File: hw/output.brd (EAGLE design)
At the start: 60.6 x 71.1 mm, 22 parts, among them Q1 MOSFET-NCHANNELFDD8780, Q2 MOSFET-NCHANNELFDD8780, U3 TMP102

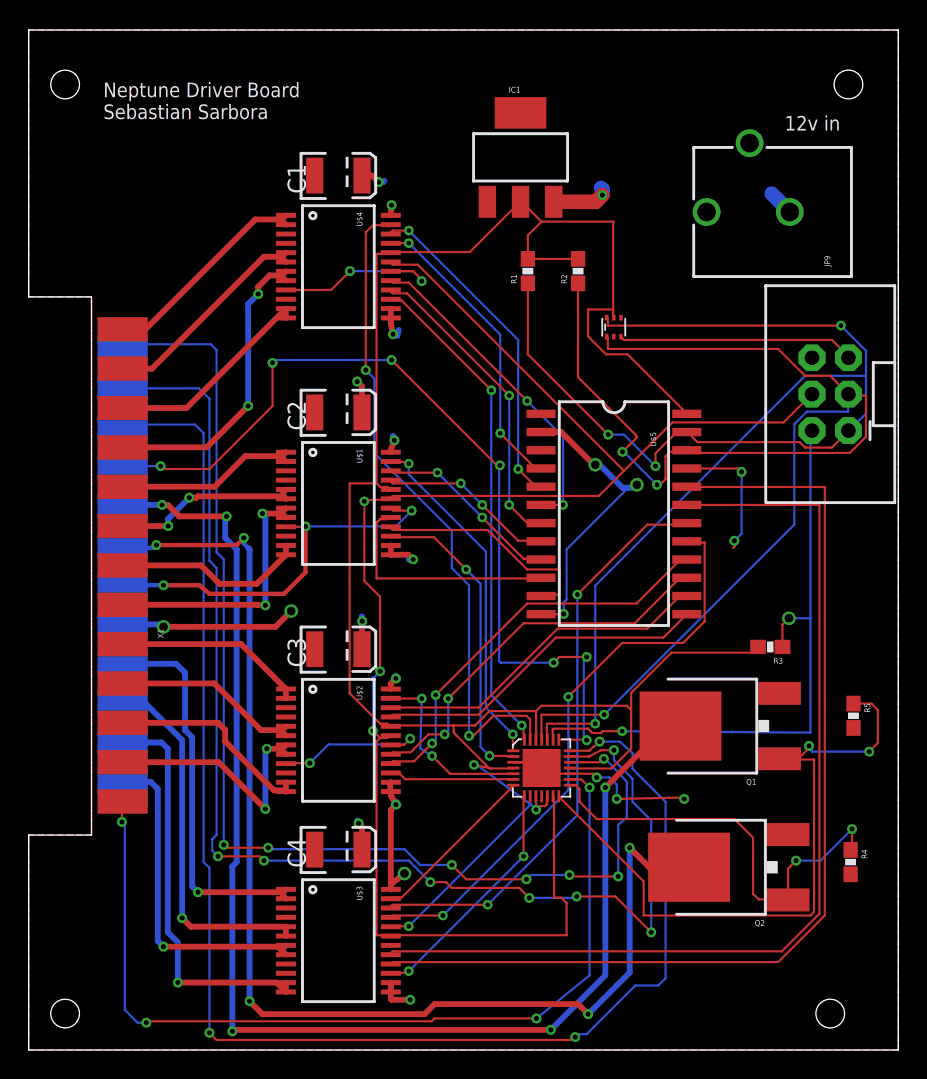
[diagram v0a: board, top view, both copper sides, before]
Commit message: Consolidated output board to use single control IC (CY8C9540A), removed servo pwm lines for this revision.
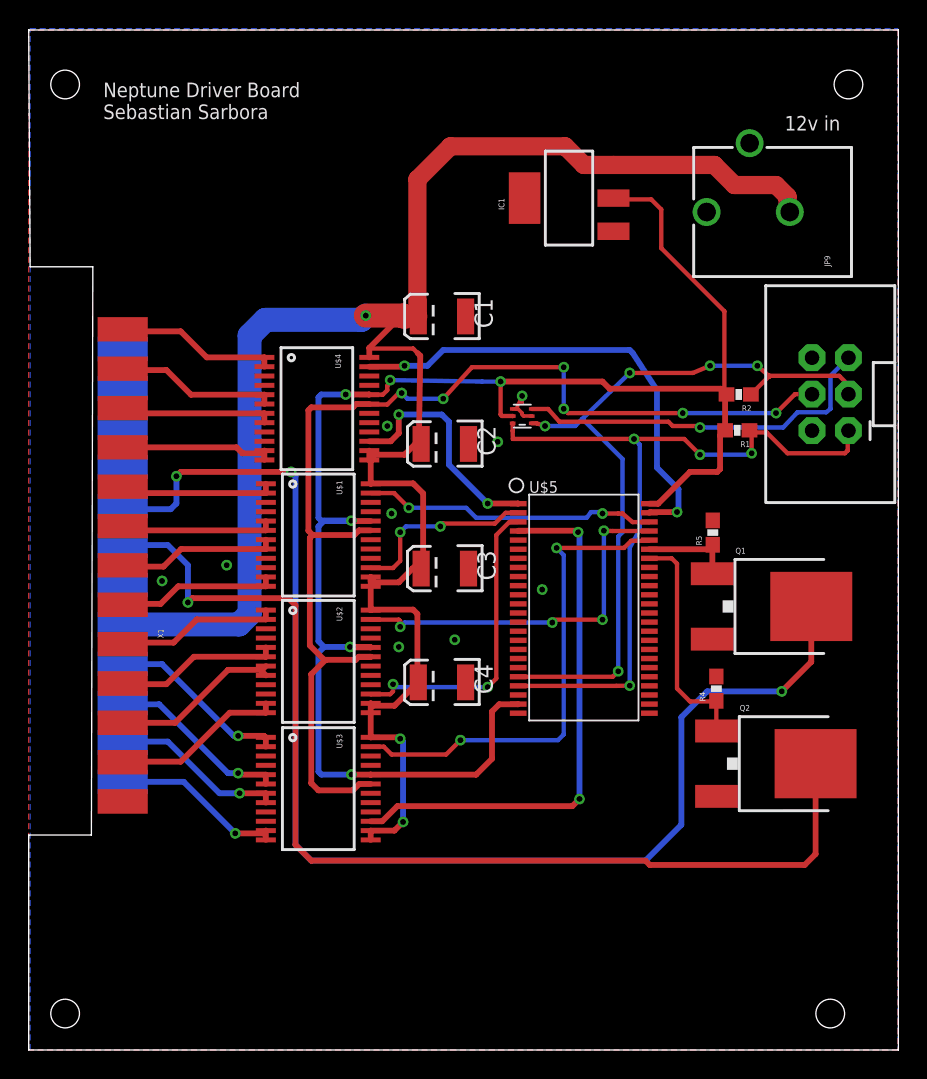
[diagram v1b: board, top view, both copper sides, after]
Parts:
- removed R3: 1K, SparkFun-Resistors:0603-RES
- removed U2: (no value), SparkFun-DigitalIC:QFN-28
- U$5: value PCF8575C -> CY8C9540A; device SparkFun-DigitalIC:SO-24DW -> SpaceY:48-SSOP-CY
- moved R1 18.3 mm to (49.4, 43.2), turned to 180 degrees
- moved R5 16.1 mm to (47.7, 36.1), turned to 90 degrees
- moved R4 15.3 mm to (47.9, 25.2), turned to 90 degrees
- moved R2 14.1 mm to (49.5, 45.7), turned to 180 degrees
- moved C4 13.7 mm to (28.8, 25.6), turned to 180 degrees
- moved C1 12.2 mm to (28.8, 51.1), turned to 180 degrees
- moved U$3 10.7 mm to (20.2, 18.2)
- moved Q1 10.2 mm to (53.0, 30.9), turned to 270 degrees
- moved U$4 10.0 mm to (20.1, 44.7)
- moved C3 9.31 mm to (29.0, 33.6), turned to 180 degrees
- moved Q2 9.16 mm to (53.3, 20.0), turned to 270 degrees
- moved U3 8.90 mm to (34.4, 44.2), turned to 90 degrees
- moved C2 7.74 mm to (29.0, 42.2), turned to 180 degrees
- moved U$5 7.21 mm to (38.7, 31.1), turned to 0 degrees
- moved U$2 5.68 mm to (20.2, 27.1)
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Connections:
- removed net N$1: U$5.1
- removed net N$42: U2.11
- removed net N$43: U2.9
- net AIN1: no longer U$5.4
- net AIN2: no longer U$5.5
- net B1: now also X1.4; no longer X1.3
- net B2: now also X1.3; no longer X1.4
- net BIN1: no longer U$5.6
- net BIN2: no longer U$5.7
- net CIN1: no longer U$5.8
- net CIN2: no longer U$5.9
- net D1: now also X1.8; no longer X1.7
- net D2: now also X1.7; no longer X1.8
- net DIN1: no longer U$5.10
- net DIN2: no longer U$5.11
- net EIN1: no longer U$5.13
- net EIN2: no longer U$5.14
- net F1: now also X1.12; no longer X1.11
- net F2: now also X1.11; no longer X1.12
- net FIN1: no longer U$5.15
- net FIN2: no longer U$5.16
- net GIN1: no longer U$5.17
- net GIN2: no longer U$5.18
- net GND: now also U$5.13, U$5.24, U$5.26; no longer U$5.12, U$5.2, U$5.21, U$5.3, U2.17, U2.29, U2.3
- net H1: now also X1.25; no longer X1.24
- net H2: now also X1.24; no longer X1.25
- net HIN1: no longer U$5.19
- net HIN2: no longer U$5.20
- net LED1: now also U$5.43; no longer U2.14
- net LED2: now also U$5.42; no longer U2.15
- net PWM_A: now also U$5.47; no longer U2.27
- net PWM_B: now also U$5.1; no longer U2.28
- net PWM_C: now also U$5.46; no longer U2.1
- net PWM_D: now also U$5.2; no longer U2.2
- net PWM_E: now also U$5.45; no longer U2.5
- net PWM_F: now also U$5.3; no longer U2.6
- net PWM_G: now also U$5.44; no longer U2.7
- net PWM_H: now also U$5.4; no longer U2.8
- net RESET: no longer R3.1, U2.23
- net SCL: now also U$5.20; no longer U$5.22, U2.25
- net SDA: now also U$5.21; no longer U$5.23, U2.24
- net SERVO1: no longer U2.16
- net SERVO2: no longer U2.19
- net SERVO3: no longer U2.20
- net SERVO4: no longer U2.21
- net SERVO5: no longer U2.22
- net STBY: no longer U2.13
- net VCC: now also U$5.23, U$5.48; no longer R3.2, U$5.24, U2.10, U2.12, U2.18, U2.26, U2.4
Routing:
- net SERVO4: track 103.3 -> 0.00 mm, vias 3 -> 0
- net GND: track 99.2 -> 3.58 mm, vias 15 -> 9
- net V_BATT: track 49.7 -> 143.1 mm, vias 15 -> 3
- net SERVO3: track 88.2 -> 0.00 mm, vias 7 -> 0
- net SERVO2: track 82.0 -> 0.00 mm, vias 7 -> 0
- net HIN2: track 71.2 -> 0.00 mm
- net HIN1: track 68.9 -> 0.00 mm
- net SERVO1: track 63.3 -> 0.00 mm, vias 4 -> 0
- net SERVO5: track 62.7 -> 0.00 mm, vias 7 -> 0
- net RESET: track 43.7 -> 0.00 mm, vias 2 -> 0
- net SDA: track 97.5 -> 54.0 mm
- net SCL: track 94.6 -> 52.8 mm, vias 3 -> 5
- net GIN1: track 41.0 -> 0.00 mm, vias 2 -> 0
- net GIN2: track 40.9 -> 0.00 mm, vias 2 -> 0
- net LED1: track 46.5 -> 6.58 mm, vias 2 -> 0
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- added copper zone on layer 16, net GND
- removed copper zone on layer 16, net V_BATT
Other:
- outline, holes or cut-outs redrawn
